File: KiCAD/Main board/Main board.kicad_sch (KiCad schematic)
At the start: 29 parts, among them J1 Conn_01x03, J10 Conn_01x03, J11 Conn_01x03, J12 Conn_01x03, J13 Conn_01x02, J14 Conn_01x02, J15 Conn_01x06, J16 Conn_01x02, J17 Conn_01x02, J18 Conn_01x05, J2 Conn_01x03, J3 Conn_01x02, J4 Conn_01x02, J5 Conn_01x03, J6 Conn_01x02, J7 Conn_01x03, J8 Conn_01x02, J9 Conn_01x03

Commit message: Schematic send to Ralph for review
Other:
- note added: "Let all custom symbols and footprints be reviewed by someone else to decrease the chance of errors."
- note removed: "Just a note"
- note removed: "Let all custom symbols and footprints be checked by someone else to decrease the chance of errors."
- note removed: "Panasonic ERA-8A series for audio path resistors C0G MLCC capacitors for audio path capacitors"
- note removed: "Point of attention"
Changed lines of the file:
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@@
     (stroke (width 0) (type default))
-  )
-  (text "Just a note" (at 177.8 171.45 0)
-    (effects (font (size 1.27 1.27)) (justify left bottom))
   )
   (text "FPGA power" (at 215.9 138.43 0)
@@
     (effects (font (size 1.27 1.27)) (justify left bottom))
   )
-  (text "Let all custom symbols and footprints be checked by someone else to decrease the chance of errors."
-    (at 72.39 158.75 0)
-    (effects (font (size 1.27 1.27) (thickness 0.254) bold (color 255 0 0 1)) (justify left bottom))
+  (text "Let all custom symbols and footprints be reviewed by someone else to decrease the chance of errors."
+    (at 41.91 161.29 0)
+    (effects (font (size 2.54 2.54) (thickness 0.254) bold (color 255 0 0 1)) (justify left bottom))
   )
   (text "DC in" (at 22.86 138.43 0)
     (effects (font (size 1.27 1.27)) (justify left bottom))
   )
-  (text "Point of attention" (at 177.8 168.91 0)
-    (effects (font (size 1.27 1.27) (color 200 0 200 1)) (justify left bottom))
-  )
-  (text "Panasonic ERA-8A series for audio path resistors\nC0G MLCC capacitors for audio path capacitors"
-    (at 177.8 180.34 0)
-    (effects (font (size 1.27 1.27)) (justify left bottom))
-  )

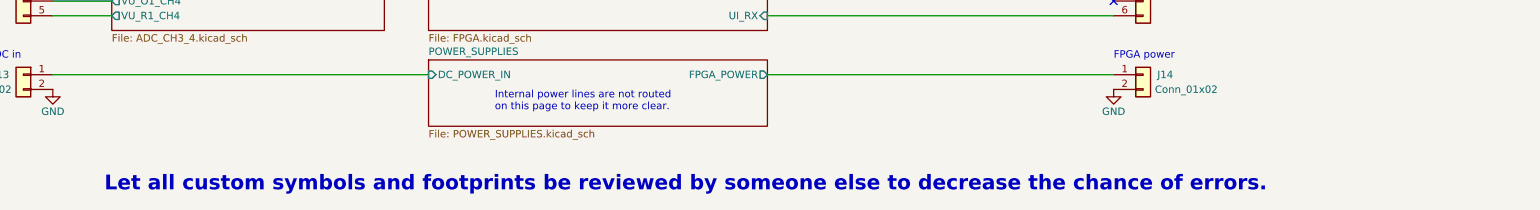
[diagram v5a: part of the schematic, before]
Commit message: Filled in main board BOM exept for fifth buck converter
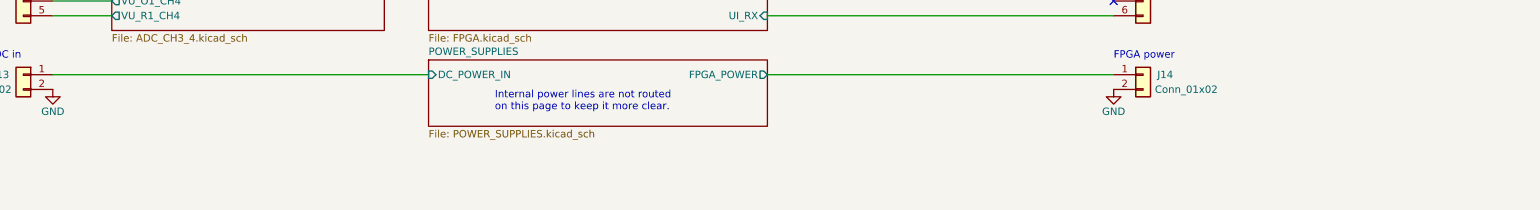
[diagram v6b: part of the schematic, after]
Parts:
- J14: footprint Connector_Phoenix_MC:PhoenixContact_MCV_1,5_2-G-3.5_1x02_P3.50mm_Vertical -> Connector_Phoenix_MC:PhoenixContact_MCV_1,5_2-G-3.81_1x02_P3.81mm_Vertical
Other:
- note removed: "Let all custom symbols and footprints be reviewed by someone else to decrease the chance of errors."
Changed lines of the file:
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@@
     (effects (font (size 1.27 1.27)) (justify left bottom))
-  )
-  (text "Let all custom symbols and footprints be reviewed by someone else to decrease the chance of errors."
-    (at 41.91 161.29 0)
-    (effects (font (size 2.54 2.54) (thickness 0.254) bold (color 255 0 0 1)) (justify left bottom))
   )
   (text "DC in" (at 22.86 138.43 0)
@@
       (effects (font (size 1.27 1.27)) (justify left))
     )
-    (property "Footprint" "Connector_Phoenix_MC:PhoenixContact_MCV_1,5_2-G-3.5_1x02_P3.50mm_Vertical" (at 220.98 140.97 0)
+    (property "Footprint" "Connector_Phoenix_MC:PhoenixContact_MCV_1,5_2-G-3.81_1x02_P3.81mm_Vertical" (at 220.98 140.97 0)
       (effects (font (size 1.27 1.27)) hide)
     )
@@
       (effects (font (size 1.27 1.27)) hide)
     )
-    (property "Datasheet" "https://www.tinytronics.nl/shop/nl/kabels-en-connectoren/connectoren/jst-compatible/jst-xh-6p-compatible-printplaatconnector-male" (at 220.98 123.19 0)
-      (effects (font (size 1.27 1.27)) hide)
-    )
+    (property "Datasheet" "https://nl.farnell.com/jst-japan-solderless-terminals/b6b-ph-k-s-lf-sn/conn-header-6pos-1row-2mm/dp/9492453?CMP=KNC-GNL-GEN-KWL-PMax-Search-TEST-1527&gclid=CjwKCAjwp6CkBhB_EiwAlQVyxW3ZvWmrnmutW4vTZLKK3_qzVj8DanLyYj1TVv-Ay70tPVQq8QpeEBoCA6UQAvD_BwE" (at 220.98 123.19 0)
+      (effects (font (size 1.27 1.27)) hide)
+    )

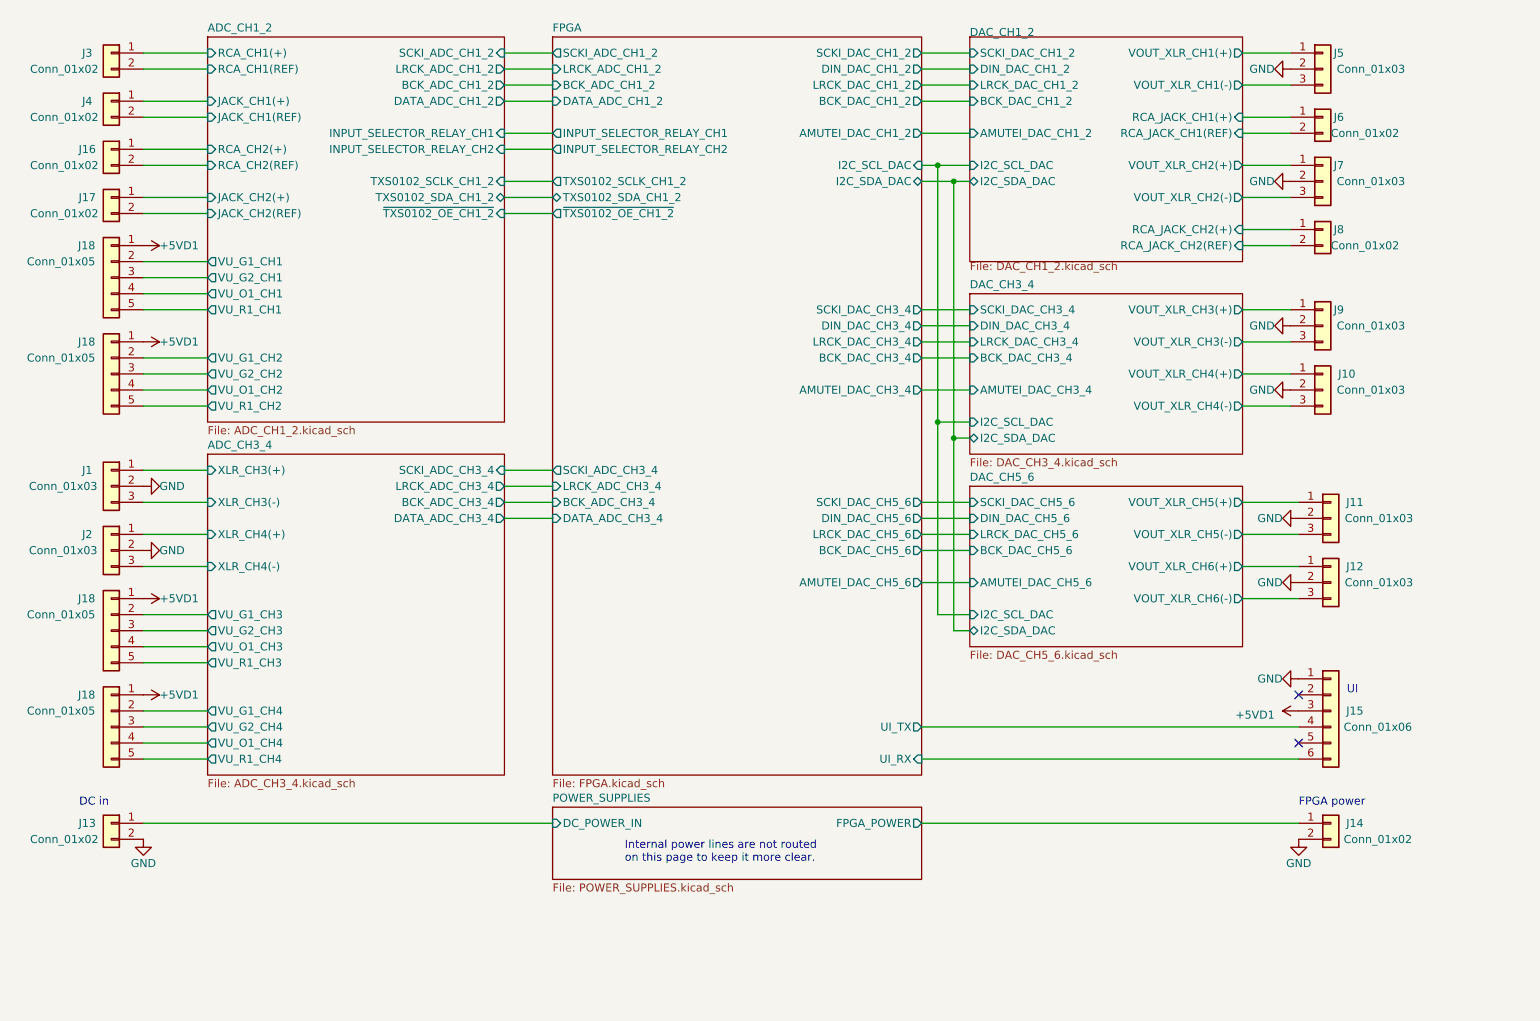
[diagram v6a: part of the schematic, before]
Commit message: Added rotary encoder and pull-up
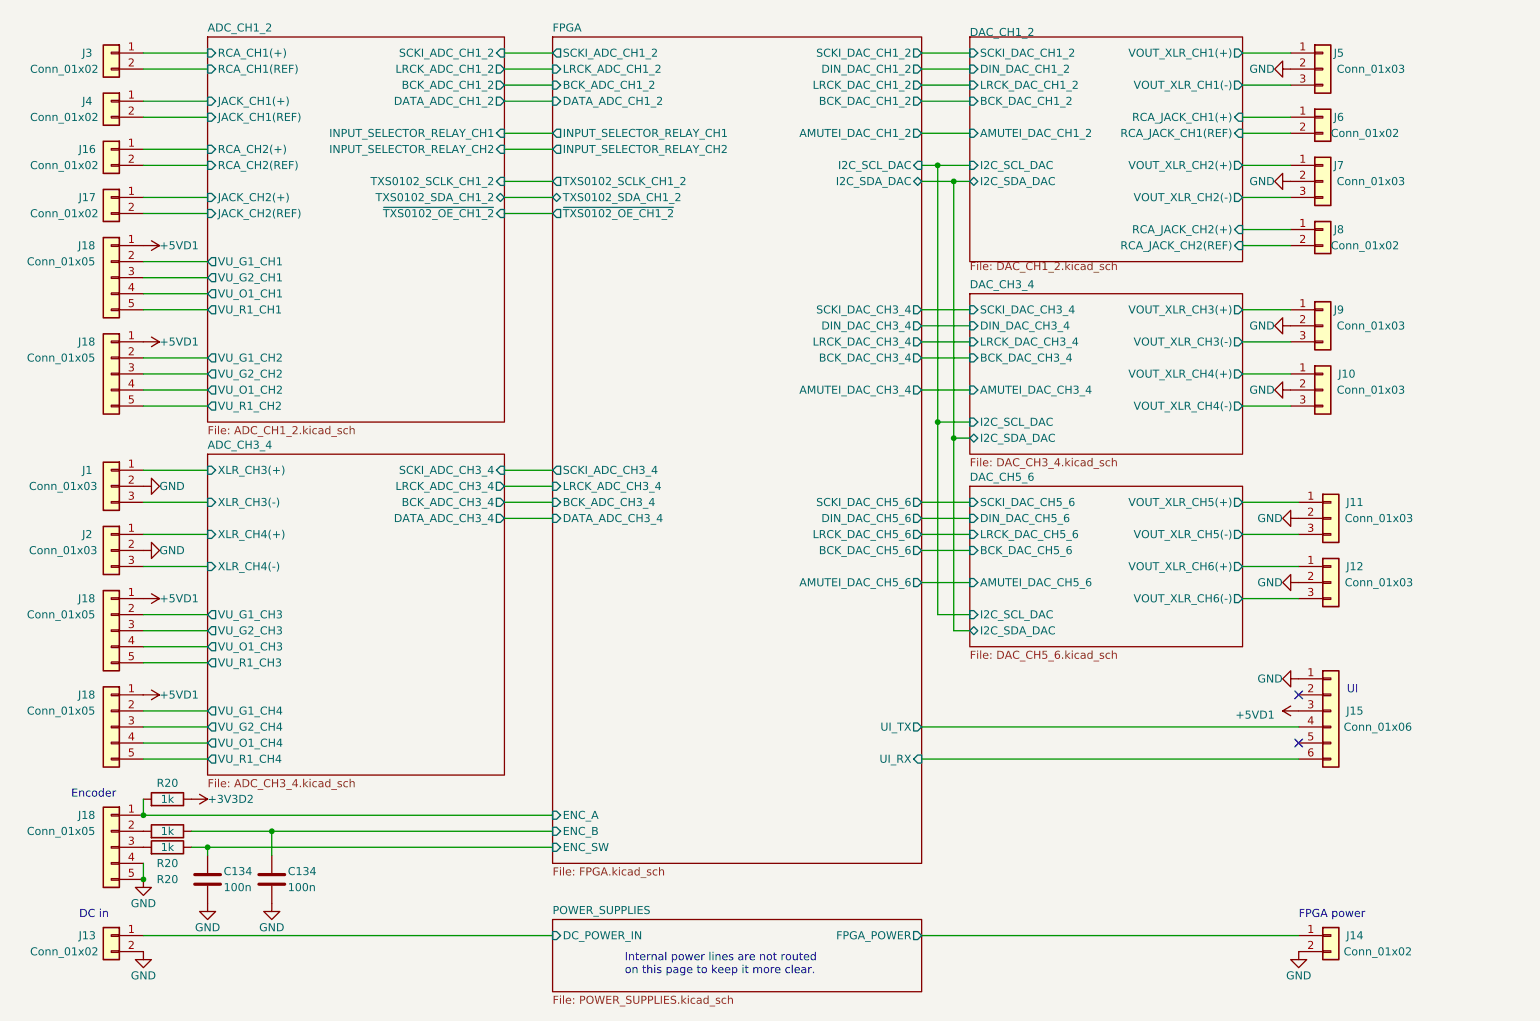
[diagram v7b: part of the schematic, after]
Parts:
- added C134 (x2): 100n, Capacitor_SMD:C_0402_1005Metric, symbol Device:C
- added J18: Conn_01x05, Connector_JST:JST_XH_B5B-XH-A_1x05_P2.50mm_Vertical, symbol Connector_Generic:Conn_01x05
- added R20 (x3): 1k, Resistor_SMD:R_0805_2012Metric, symbol Device:R
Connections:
- net GND: now also C134.2, C134.2, J18.4 (Pin_4), J18.5 (Pin_5)
- new net: J18.3 (Pin_3), R20.2
- new net: J18.2 (Pin_2), R20.2
- new net +3V3D2: R20.1
- new net FPGA/ENC_A: J18.1 (Pin_1), R20.2
- new net FPGA/ENC_B: C134.1, R20.1
- new net FPGA/ENC_SW: C134.1, R20.1
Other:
- sheet FPGA ports: added ENC_A, ENC_B, ENC_SW; removed none
- note added: "Encoder"
- moved on the sheet: J13, J14

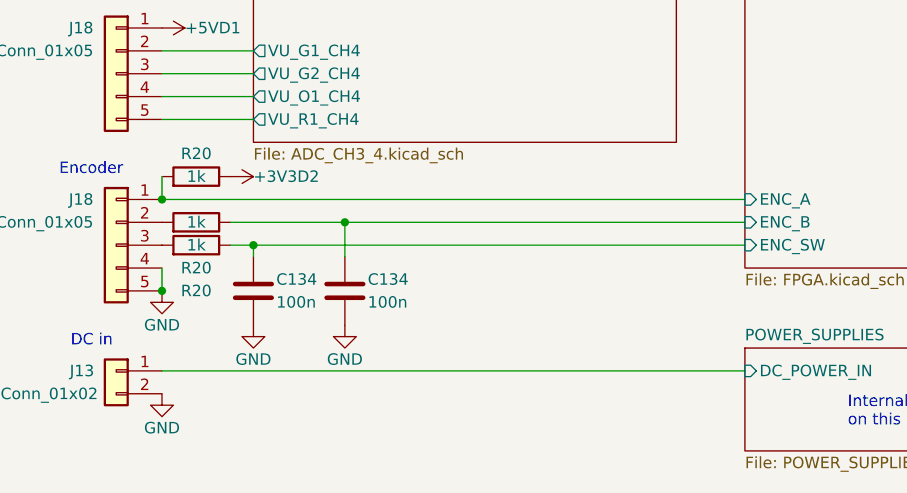
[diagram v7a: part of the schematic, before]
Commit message: updated the encoder schematic
added pullup resistors to the output lines of the encoder and added debounce to the last remaining line.
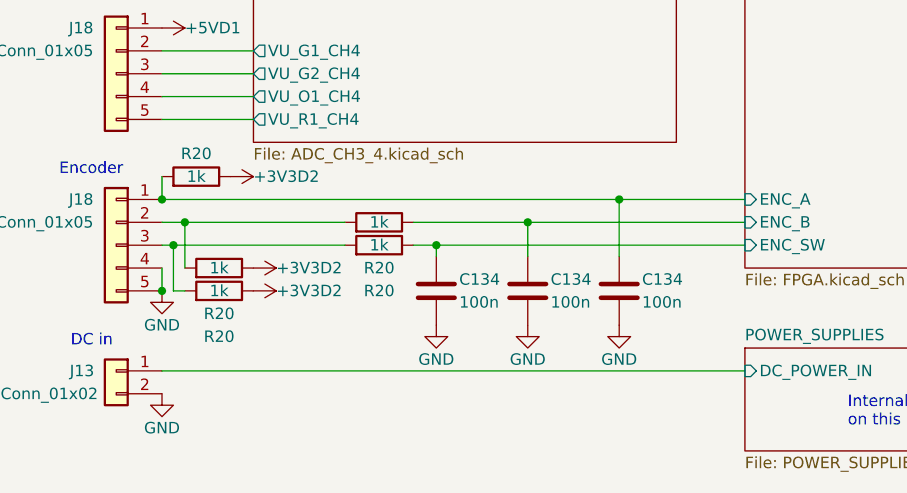
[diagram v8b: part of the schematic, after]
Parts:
- added C134: 100n, Capacitor_SMD:C_0402_1005Metric, symbol Device:C
- added R20 (x2): 1k, Resistor_SMD:R_0805_2012Metric, symbol Device:R
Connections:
- net +3V3D2: now also R20.1, R20.1
- net FPGA/ENC_A: now also C134.1
- net GND: now also C134.2
- net at J18.3 (Pin_3), R20.2: now also R20.2
- net at J18.2 (Pin_2), R20.2: now also R20.2
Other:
- moved on the sheet: C134, R20
